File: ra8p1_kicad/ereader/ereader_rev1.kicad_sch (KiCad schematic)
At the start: 0 parts

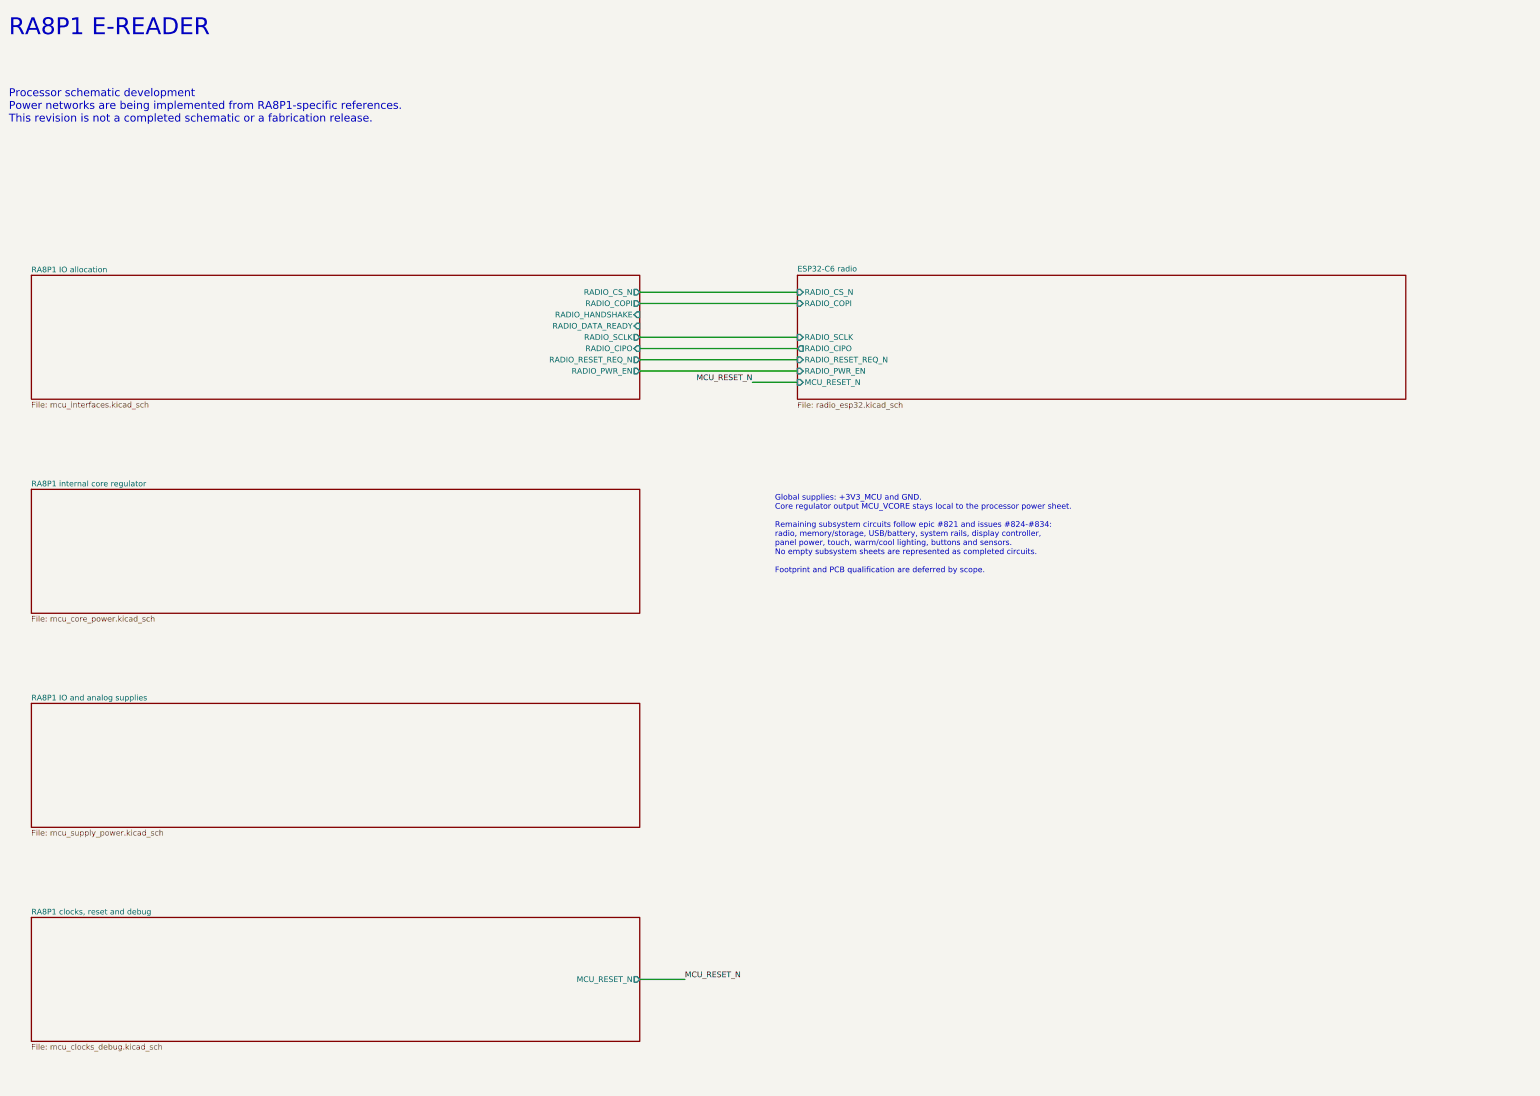
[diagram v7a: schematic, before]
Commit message: Wire e-reader user controls and record power architecture
Connect four protected page/volume inputs and power INT/KILL interfaces through the native hierarchy. Include exact sourcing, linked calculations, local symbols, expanded requirements, and a fresh eight-page PDF and full BOM.

Progress checkpoint, not fabrication release: power source, EN supervision and discharge remain unfinished. Configured ERC: 204 errors and 2 warnings, versus 208 and 2 at the previous checkpoint; six MCU disconnections resolved and two explicit power-draft gaps added. Page/volume sheet has zero findings. One independent review round: no findings. Arithmetic, netlist/BOM consistency and all PDF pages reviewed. Hardware-only hook bypass explicitly authorized.
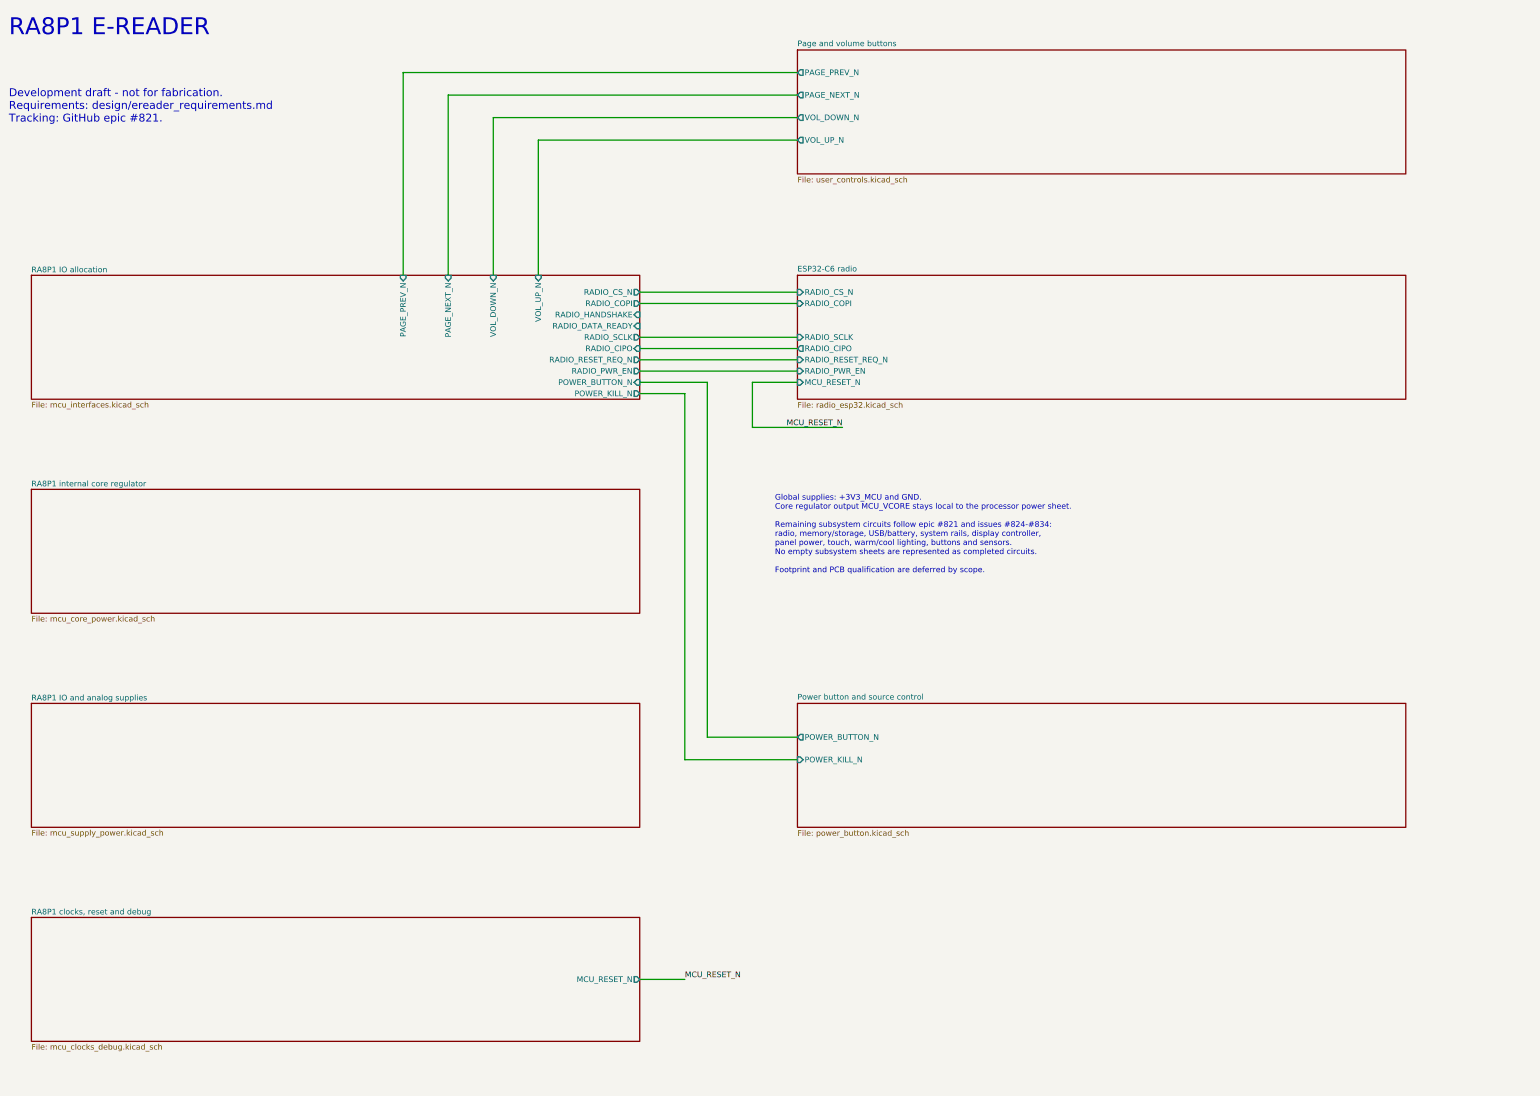
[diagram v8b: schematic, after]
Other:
- added sheet Page and volume buttons (user_controls.kicad_sch)
- added sheet Power button and source control (power_button.kicad_sch)
- sheet RA8P1 IO allocation ports: added PAGE_NEXT_N, PAGE_PREV_N, POWER_BUTTON_N, POWER_KILL_N, VOL_DOWN_N, VOL_UP_N; removed none
- note added: "Development draft - not for fabrication. Requirements: design/ereader_requirements.md Tracking: GitHub epic #821."
- note removed: "Processor schematic development Power networks are being implemented from RA8P1-specific references. This revision is not a completed schematic or a fabrication release."
